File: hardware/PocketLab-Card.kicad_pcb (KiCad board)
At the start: 4 copper layers, 85.6 x 54 mm, 0 parts

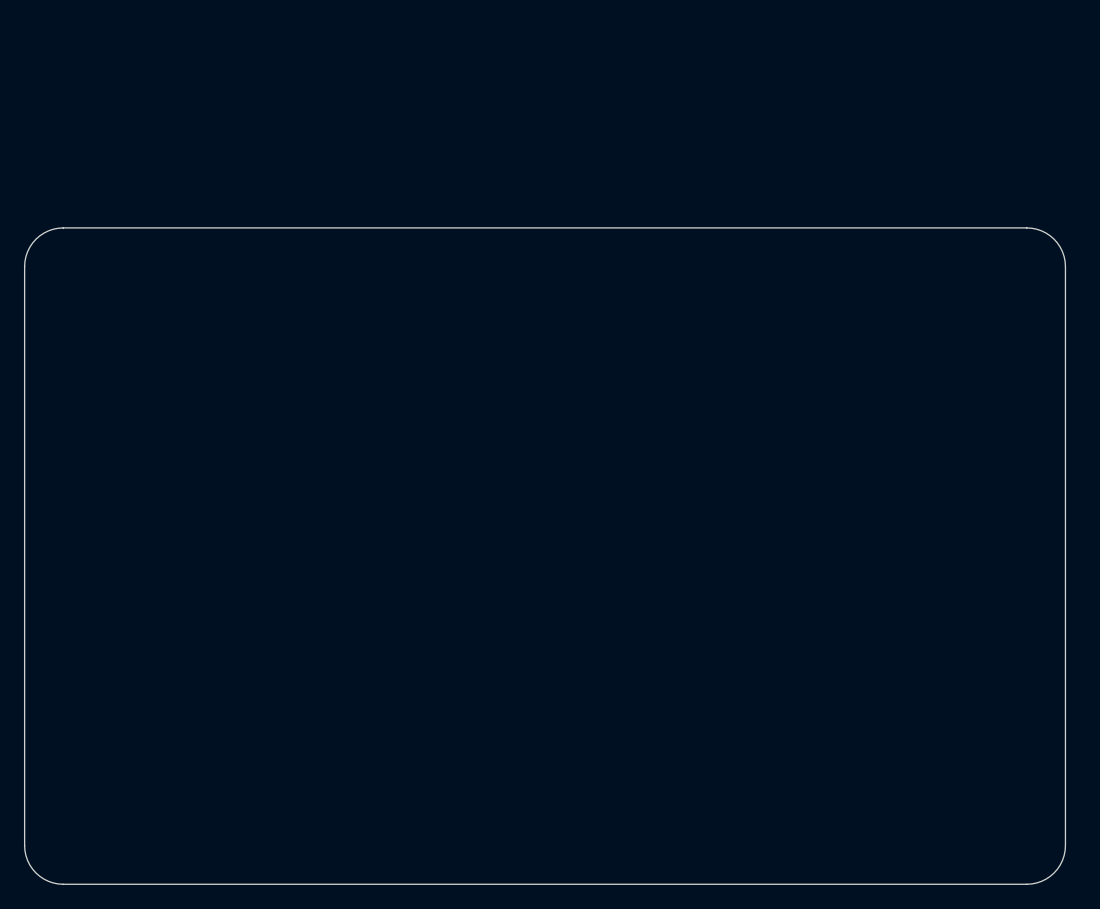
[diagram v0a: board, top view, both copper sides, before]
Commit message: Add physical component placement draft
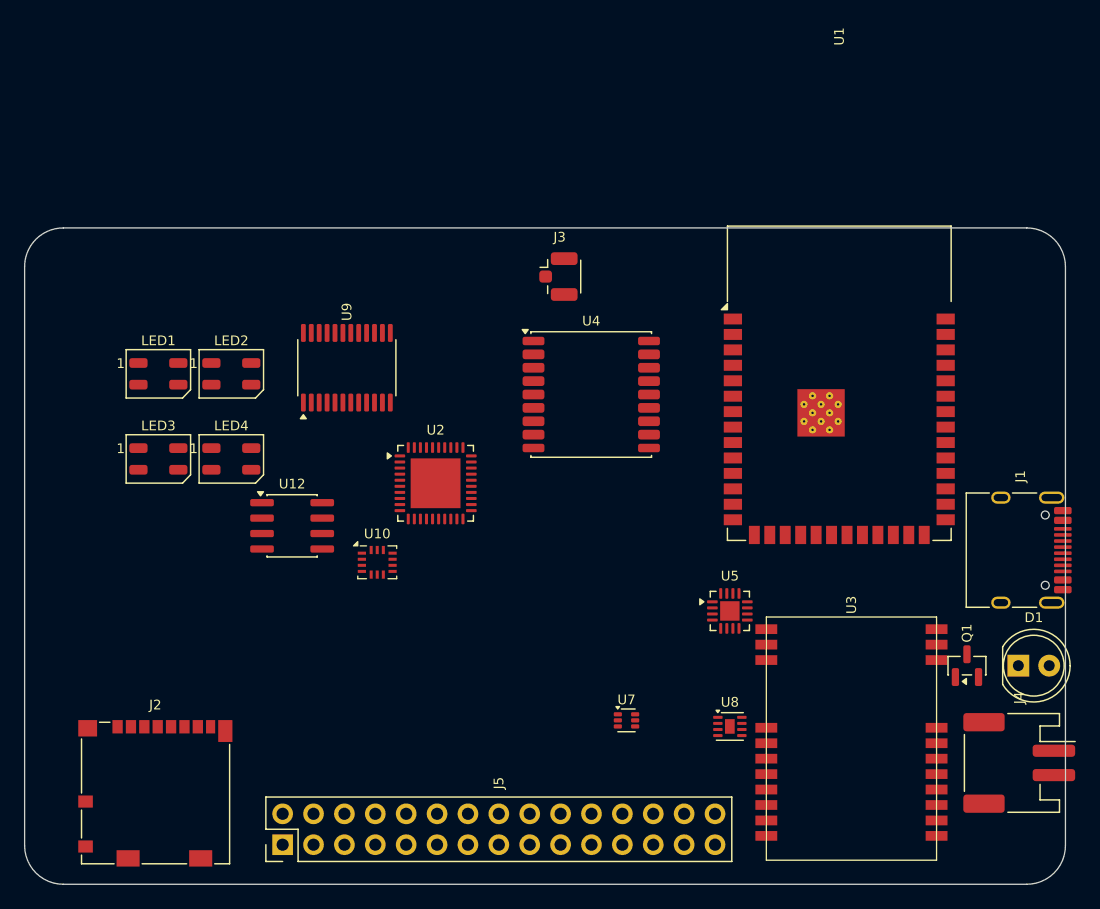
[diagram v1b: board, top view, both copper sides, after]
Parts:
- added D1: TSAL6200 940nm IR (bend toward edge), LED_THT:LED_D5.0mm, F.Cu at (101.7, 56.0)
- added J1: USB-C data/power, Connector_USB:USB_C_Receptacle_HRO_TYPE-C-31-M-12, F.Cu at (101.3, 46.5)
- added J2: microSD, Connector_Card:microSD_HC_Molex_104031-0811, F.Cu at (30.8, 66.5)
- added J3: GNSS ANT, Connector_Coaxial:U.FL_Hirose_U.FL-R-SMT-1_Vertical, F.Cu at (64.4, 24.0)
- added J4: BAT 1S 3.7V, Connector_JST:JST_PH_S2B-PH-SM4-TB_1x02-1MP_P2.00mm_Horizontal, F.Cu at (101.8, 64.0)
- added J5: 2x15 2.54mm EXPANSION, Connector_PinHeader_2.54mm:PinHeader_2x15_P2.54mm_Vertical, F.Cu at (41.2, 70.7)
- added LED1: WS2812B-MINI-V3, LED_SMD:LED_WS2812B-Mini_PLCC4_3.5x3.5mm, F.Cu at (31.0, 32.0)
- added LED2: WS2812B-MINI-V3, LED_SMD:LED_WS2812B-Mini_PLCC4_3.5x3.5mm, F.Cu at (37.0, 32.0)
- added LED3: WS2812B-MINI-V3, LED_SMD:LED_WS2812B-Mini_PLCC4_3.5x3.5mm, F.Cu at (31.0, 39.0)
- added LED4: WS2812B-MINI-V3, LED_SMD:LED_WS2812B-Mini_PLCC4_3.5x3.5mm, F.Cu at (37.0, 39.0)
- added Q1: AO3400A IR driver, Package_TO_SOT_SMD:SOT-23, F.Cu at (97.5, 56.0)
- added U1: ESP32-S3-WROOM-1-N8R2, RF_Module:ESP32-S3-WROOM-1, F.Cu at (87.0, 32.8)
- added U10: BMI270 (FULL option), Package_LGA:Bosch_LGA-14_3x2.5mm_P0.5mm, F.Cu at (49.0, 47.5)
- added U12: PCF8563T, Package_SO:SOIC-8_3.9x4.9mm_P1.27mm, F.Cu at (42.0, 44.5)
- added U2: PN5321A3HN/C106, Package_DFN_QFN:HVQFN-40-1EP_6x6mm_P0.5mm_EP4.1x4.1mm, F.Cu at (53.8, 41.0)
- added U3: E07-900M10S, PocketLab_Custom:E07-900M10S, F.Cu at (81.0, 53.0)
- added U4: MAX-M10S-00B, RF_GPS:ublox_MAX, F.Cu at (66.6, 33.7)
- added U5: BQ24074RGTR, Package_DFN_QFN:VQFN-16-1EP_3x3mm_P0.5mm_EP1.6x1.6mm, F.Cu at (78.0, 51.5)
- added U7: TPS61023DRLR, Package_TO_SOT_SMD:SOT-563, F.Cu at (69.5, 60.5)
- added U8: MAX17048G+T10, Package_DFN_QFN:TDFN-8-1EP_2x2mm_P0.5mm_EP0.8x1.2mm, F.Cu at (78.0, 61.0)
- added U9: TCA9535PWR, Package_SO:TSSOP-24_4.4x7.8mm_P0.65mm, F.Cu at (46.5, 31.5)
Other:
- board text added: "NFC LOOP RESERVE - NOT ROUTED"
- board text added: "PLACEMENT DRAFT - UNROUTED / NOT FOR PRODUCTION"
- board text added: "POWER ISLAND"
- board text added: "U11 BMP390"
- board text added: "U13 IR RX"
- board text added: "U6 TPS63070 + L"
- board text removed: "POCKETLAB CARD V1 - MECHANICAL SCAFFOLD"

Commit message: Publish current PocketLab Card hardware checkpoint
Publishes the current hardware and documentation checkpoint while removing obsolete renders, empty placeholder sheets, generated PCB/autorouter intermediates, and duplicate staging reports. Generated staging artifacts remain reproducible from the checked-in scripts.
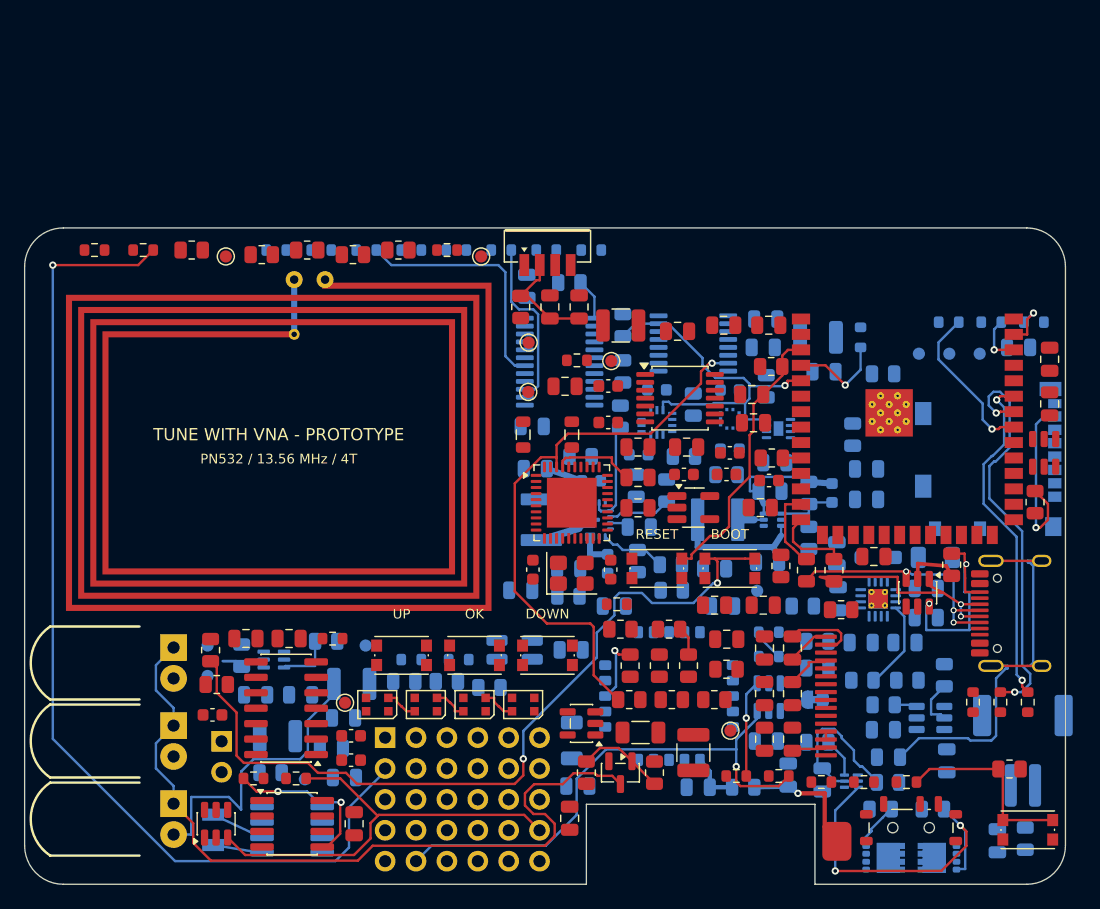
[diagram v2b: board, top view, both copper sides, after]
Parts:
- added A1: T3-868M SPRING ANTENNA, PocketLab_Custom:T3-868M_Edge_Solder, F.Cu at (86.8, 70.5)
- added AE1: PCB NFC LOOP - TUNE ON V1, PocketLab_Custom:NFC_Loop_35x27mm_4T_TUNE, F.Cu at (40.9, 38.0)
- added C101: 4.7nF 1kV, Capacitor_SMD:C_0805_2012Metric, B.Cu at (91.0, 63.5)
- added C102: 100nF, Capacitor_SMD:C_0805_2012Metric, B.Cu at (85.6, 65.4)
- added C103: 4.7uF 10V, Capacitor_SMD:C_0805_2012Metric, B.Cu at (94.2, 52.0)
- added C104: 22uF 10V, Capacitor_SMD:C_0805_2012Metric, B.Cu at (92.4, 54.1)
- added C105: 4.7uF 10V, Capacitor_SMD:C_0805_2012Metric, B.Cu at (86.9, 50.5)
- added C106: 100nF, Capacitor_SMD:C_0805_2012Metric, B.Cu at (94.2, 49.6)
- added C107: 100nF, Capacitor_SMD:C_0805_2012Metric, B.Cu at (70.5, 44.6)
- added C108: 10uF, Capacitor_SMD:C_0805_2012Metric, B.Cu at (62.0, 39.8)
- added C109: 10uF DNP - populate only after VSYS stability test, Capacitor_SMD:C_0805_2012Metric, B.Cu at (80.7, 29.8)
- added C110: 22uF, Capacitor_SMD:C_0805_2012Metric, B.Cu at (60.8, 49.8)
- added C111: 22uF, Capacitor_SMD:C_0805_2012Metric, B.Cu at (61.7, 36.3)
- added C112: 22uF, Capacitor_SMD:C_0805_2012Metric, B.Cu at (68.5, 51.1)
- added C113: 220pF C0G, Capacitor_SMD:C_0603_1608Metric, B.Cu at (86.4, 41.8)
- added C114: 10uF, Capacitor_SMD:C_0805_2012Metric, B.Cu at (81.1, 47.5)
- added C115: 22uF, Capacitor_SMD:C_0805_2012Metric, B.Cu at (81.3, 41.6)
- added C116: 22uF, Capacitor_SMD:C_0805_2012Metric, B.Cu at (77.4, 51.1)
- added C117: 10uF, Capacitor_SMD:C_0805_2012Metric, B.Cu at (90.6, 61.3)
- added C118: 100nF, Capacitor_SMD:C_0805_2012Metric, B.Cu at (100.0, 70.4)
- added C119: 10uF, Capacitor_SMD:C_0805_2012Metric, B.Cu at (95.8, 63.8)
- added C120: 100nF, Capacitor_SMD:C_0805_2012Metric, B.Cu at (81.7, 39.3)
- added C121: 100nF, Capacitor_SMD:C_0805_2012Metric, B.Cu at (88.8, 54.1)
- added C122: 100nF, Capacitor_SMD:C_0805_2012Metric, B.Cu at (86.8, 46.8)
- added C123: 10uF 25V X5R HF, Capacitor_SMD:C_0603_1608Metric, B.Cu at (66.6, 40.8)
- added C124: 10uF 25V X5R HF, Capacitor_SMD:C_0603_1608Metric, B.Cu at (68.0, 47.6)
- added C201: 1uF, Capacitor_SMD:C_0805_2012Metric, F.Cu at (79.8, 33.7)
- added C202: 10uF, Capacitor_SMD:C_0805_2012Metric, F.Cu at (81.2, 28.0)
- added C203: 100nF, Capacitor_SMD:C_0805_2012Metric, F.Cu at (77.5, 28.0)
- added C301: 100nF, Capacitor_SMD:C_0805_2012Metric, F.Cu at (64.4, 33.0)
- added C302: 100nF AVDD, Capacitor_SMD:C_0805_2012Metric, F.Cu at (79.9, 36.0)
- added C303: 4.7uF VBAT bulk, Capacitor_SMD:C_0805_2012Metric, F.Cu at (70.4, 38.0)
- added C304: 100nF, Capacitor_SMD:C_0805_2012Metric, F.Cu at (74.4, 38.0)
- added C305: 100nF, Capacitor_SMD:C_0805_2012Metric, F.Cu at (70.4, 40.5)
- added C306: 22pF C0G, Capacitor_SMD:C_0603_1608Metric, F.Cu at (61.8, 48.1)
- added C307: 22pF C0G, Capacitor_SMD:C_0603_1608Metric, F.Cu at (68.2, 48.1)
- added C308: 220pF C0G, Capacitor_SMD:C_0603_1608Metric, F.Cu at (68.0, 36.0)
- added C309: 220pF C0G, Capacitor_SMD:C_0603_1608Metric, F.Cu at (68.0, 33.0)
- added C310: DNP MATCH, Capacitor_SMD:C_0603_1608Metric, F.Cu at (74.2, 40.3)
- added C311: DNP MATCH, Capacitor_SMD:C_0603_1608Metric, F.Cu at (78.0, 38.5)
- added C312: DNP MATCH, Capacitor_SMD:C_0603_1608Metric, F.Cu at (77.7, 40.3)
- added C313: 10uF DVDD bulk, Capacitor_SMD:C_0805_2012Metric, F.Cu at (70.4, 43.0)
- added C314: 100nF TVDD, Capacitor_SMD:C_0805_2012Metric, F.Cu at (89.8, 47.0)
- added C315: 4.7uF TVDD bulk, Capacitor_SMD:C_0805_2012Metric, F.Cu at (76.7, 51.0)
- added C316: 100nF PVDD, Capacitor_SMD:C_0805_2012Metric, F.Cu at (80.7, 51.0)
- added C317: 100nF VBAT, Capacitor_SMD:C_0805_2012Metric, F.Cu at (77.7, 53.8)
- added C318: 1nF C0G RX COUPLING, Capacitor_SMD:C_0603_1608Metric, F.Cu at (81.2, 40.8)
- added C401: 100nF, Capacitor_SMD:C_0805_2012Metric, B.Cu at (64.7, 48.0)
- added C402: 4.7uF, Capacitor_SMD:C_0805_2012Metric, B.Cu at (76.7, 48.0)
- added C403: DNP SUBGHZ MATCH, Capacitor_SMD:C_0805_2012Metric, B.Cu at (75.4, 66.0)
- added C404: DNP SUBGHZ MATCH, Capacitor_SMD:C_0805_2012Metric, B.Cu at (82.8, 65.0)
- added C501: 100nF HTRC supply, Capacitor_SMD:C_0805_2012Metric, B.Cu at (39.0, 58.4)
- added C502: 10uF HTRC pulse reservoir, Capacitor_SMD:C_0805_2012Metric, B.Cu at (42.7, 58.4)
- added C503: 100nF CEXT, Capacitor_SMD:C_0805_2012Metric, F.Cu at (38.2, 53.8)
- added C504: 100nF QGND, Capacitor_SMD:C_0805_2012Metric, F.Cu at (41.8, 53.8)
- added C505: 100nF C0G COIL ISOLATION, Capacitor_SMD:C_0805_2012Metric, B.Cu at (46.2, 60.3)
- added C506: 3.9nF C0G LF RESONANCE, Capacitor_SMD:C_0805_2012Metric, B.Cu at (45.2, 62.8)
- added C507: 100pF C0G DNP LF TUNE, Capacitor_SMD:C_0603_1608Metric, F.Cu at (46.9, 61.8)
- added C508: 220pF C0G DNP LF TUNE, Capacitor_SMD:C_0603_1608Metric, F.Cu at (46.9, 63.8)
- added C509: 10pF C0G DNP RX EMI, Capacitor_SMD:C_0603_1608Metric, F.Cu at (35.5, 60.0)
- added C510: 100nF, Capacitor_SMD:C_0805_2012Metric, F.Cu at (104.3, 34.5)
- added C511: 10uF, Capacitor_SMD:C_0805_2012Metric, F.Cu at (104.3, 30.8)
- added C512: 47uF 6.3V LOW-ESR, Capacitor_SMD:C_1210_3225Metric, B.Cu at (85.2, 29.0)
- added C513: 100nF OSC supply, Capacitor_SMD:C_0805_2012Metric, B.Cu at (65.0, 54.7)
- added C515: 100nF AHCT supply, Capacitor_SMD:C_0805_2012Metric, F.Cu at (73.7, 28.5)
- added C516: 100nF LVC supply, Capacitor_SMD:C_0805_2012Metric, F.Cu at (80.5, 43.0)
- added C517: 100nF secure element, Capacitor_SMD:C_0805_2012Metric, F.Cu at (47.1, 69.0)
- added C601: 100nF, Capacitor_SMD:C_0805_2012Metric, F.Cu at (63.2, 26.5)
- added C602: 4.7uF, Capacitor_SMD:C_0805_2012Metric, F.Cu at (65.6, 26.5)
- added C603: 100nF, Capacitor_SMD:C_0805_2012Metric, B.Cu at (101.7, 29.8)
- added C604: 100nF, Capacitor_SMD:C_0805_2012Metric, B.Cu at (85.7, 31.8)
- added C605: 100nF, Capacitor_SMD:C_0805_2012Metric, B.Cu at (89.2, 39.8)
- added C606: 100nF, Capacitor_SMD:C_0805_2012Metric, B.Cu at (89.2, 42.3)
- added C607: 22uF 10V X5R IR BUFFER, Capacitor_SMD:C_1206_3216Metric, F.Cu at (70.7, 61.5)
- added C608: 100nF IR HF, Capacitor_SMD:C_0805_2012Metric, F.Cu at (64.8, 68.5)
- added C609: 100nF X7R, Capacitor_SMD:C_0805_2012Metric, B.Cu at (65.5, 65.9)
- added C610: 1uF X7R, Capacitor_SMD:C_0805_2012Metric, F.Cu at (83.2, 54.5)
- added C611: 1uF X7R, Capacitor_SMD:C_0805_2012Metric, F.Cu at (83.2, 58.3)
- added C612: 100nF X7R, Capacitor_SMD:C_0805_2012Metric, F.Cu at (80.8, 54.5)
- added C613: 4.7uF X5R, Capacitor_SMD:C_0805_2012Metric, F.Cu at (80.8, 58.3)
- added C614: 2.2uF X7R, Capacitor_SMD:C_0805_2012Metric, F.Cu at (83.2, 62.0)
- added C615: 4.7uF X5R, Capacitor_SMD:C_0805_2012Metric, F.Cu at (80.8, 62.0)
- added C616: 100nF X7R, Capacitor_SMD:C_0805_2012Metric, B.Cu at (81.0, 62.2)
- added C617: 22uF 10V X5R IR BUFFER, Capacitor_SMD:C_1206_3216Metric, B.Cu at (65.0, 62.1)
- added C701: 100nF, Capacitor_SMD:C_0805_2012Metric, B.Cu at (61.3, 24.8)
- added C702: 100nF, Capacitor_SMD:C_0603_1608Metric, B.Cu at (70.5, 38.6)
- added C703: 100nF, Capacitor_SMD:C_0603_1608Metric, B.Cu at (72.0, 33.3)
- added C704: 100nF, Capacitor_SMD:C_0603_1608Metric, B.Cu at (78.0, 33.3)
- added C705: 100nF, Capacitor_SMD:C_0603_1608Metric, B.Cu at (78.0, 38.2)
- added C706: 100nF, Capacitor_SMD:C_0805_2012Metric, B.Cu at (46.3, 65.2)
- added C707: 100nF, Capacitor_SMD:C_0805_2012Metric, B.Cu at (81.0, 27.5)
- added D101: SMF5.0A, Diode_SMD:D_SOD-123F, B.Cu at (90.2, 47.1)
- added D2: TSAL6200 940nm, PocketLab_Custom:TSAL6200_LayFlat_Inboard, F.Cu at (20.2, 62.2)
- added D3: TSAL6200 940nm, PocketLab_Custom:TSAL6200_LayFlat_Inboard, F.Cu at (20.2, 68.6)
- added F1: Littelfuse 1206L075/13.2, Fuse:Fuse_1206_3216Metric, B.Cu at (94.9, 47.1)
- added J8: ER-OLED0.42-1W 72x40 SSD1306B, PocketLab_Custom:EastRising_ER-OLED0.42-1W_SolderFPC, F.Cu at (90.5, 58.5)
- added L301: 560nH C0G/Q, Inductor_SMD:L_0805_2012Metric, F.Cu at (61.0, 37.0)
- added L302: 560nH C0G/Q, Inductor_SMD:L_0805_2012Metric, F.Cu at (65.0, 37.0)
- added L6: 1.5uH XFL4020-152ME, PocketLab_Custom:Coilcraft_XFL4020, B.Cu at (62.5, 44.0)
- added L7: 1uH HBME042A, PocketLab_Custom:Cyntec_HBME042A-1R0MS, B.Cu at (77.0, 44.0)
- added Q2: CSD16406Q3 DISCHARGE, PocketLab_Custom:CSD16406Q3_VSON-8_3.3x3.3mm_P0.65mm_JLC, B.Cu at (95.2, 71.8)
- added Q3: CSD16406Q3 CHARGE, PocketLab_Custom:CSD16406Q3_VSON-8_3.3x3.3mm_P0.65mm_JLC, B.Cu at (90.7, 71.8)
- added R101: 5.1k 1%, Resistor_SMD:R_0805_2012Metric, B.Cu at (102.3, 70.2)
- added R102: 5.1k 1%, Resistor_SMD:R_0805_2012Metric, F.Cu at (96.2, 47.7)
- added R103: 1M, Resistor_SMD:R_0805_2012Metric, B.Cu at (65.7, 38.8)
- added R104: 330R, Resistor_SMD:R_0805_2012Metric, B.Cu at (91.0, 65.6)
- added R105: 2.2k, Resistor_SMD:R_0805_2012Metric, B.Cu at (85.2, 62.3)
- added R106: 5.1M, Resistor_SMD:R_0805_2012Metric, B.Cu at (94.7, 67.8)
- added R107: 5.1M, Resistor_SMD:R_0805_2012Metric, B.Cu at (90.4, 67.8)
- added R108: 10k TS fixed, Resistor_SMD:R_0805_2012Metric, B.Cu at (74.2, 38.8)
- added R109: 100k, Resistor_SMD:R_0805_2012Metric, B.Cu at (77.7, 40.3)
- added R110: 100k, Resistor_SMD:R_0805_2012Metric, B.Cu at (73.2, 49.8)
- added R111: 3.48k 1%, Resistor_SMD:R_0805_2012Metric, B.Cu at (85.2, 54.0)
- added R112: 3.01k 1%, Resistor_SMD:R_0805_2012Metric, B.Cu at (85.2, 56.2)
- added R113: 1.78k 1%, Resistor_SMD:R_0805_2012Metric, B.Cu at (88.9, 57.2)
- added R114: 68.1k 1%, Resistor_SMD:R_0805_2012Metric, B.Cu at (92.6, 57.2)
- added R115: 100k, Resistor_SMD:R_0805_2012Metric, B.Cu at (64.7, 50.3)
- added R116: 10k, Resistor_SMD:R_0805_2012Metric, B.Cu at (70.3, 41.2)
- added R117: 470k 1%, Resistor_SMD:R_0805_2012Metric, B.Cu at (70.4, 47.4)
- added R118: 150k 1%, Resistor_SMD:R_0805_2012Metric, B.Cu at (73.2, 47.7)
- added R119: 10k, Resistor_SMD:R_0805_2012Metric, B.Cu at (72.8, 41.6)
- added R120: 732k 1%, Resistor_SMD:R_0805_2012Metric, B.Cu at (84.5, 41.8)
- added R121: 100k 1%, Resistor_SMD:R_0805_2012Metric, B.Cu at (84.5, 45.5)
- added R122: 100k, Resistor_SMD:R_0805_2012Metric, B.Cu at (84.0, 51.1)
- added R123: 60.4k 1%, Resistor_SMD:R_0805_2012Metric, B.Cu at (95.6, 56.8)
- added R124: 100k, Resistor_SMD:R_0805_2012Metric, B.Cu at (88.1, 37.0)
- added R125: 10k, Resistor_SMD:R_0805_2012Metric, B.Cu at (81.0, 33.0)
- added R126: 100k, Resistor_SMD:R_0805_2012Metric, B.Cu at (75.0, 34.5)
- added R127: 100k, Resistor_SMD:R_0805_2012Metric, B.Cu at (90.7, 59.2)
- added R128: 100k, Resistor_SMD:R_0805_2012Metric, B.Cu at (90.6, 32.0)
- added R201: 22R, Resistor_SMD:R_0805_2012Metric, F.Cu at (84.3, 48.1)
- added R202: 22R, Resistor_SMD:R_0805_2012Metric, F.Cu at (86.6, 48.1)
- added R203: 10k, Resistor_SMD:R_0805_2012Metric, F.Cu at (81.4, 31.4)
- added R204: 10k, Resistor_SMD:R_0805_2012Metric, F.Cu at (35.3, 54.7)
- added R301: 10k, Resistor_SMD:R_0805_2012Metric, F.Cu at (77.7, 56.3)
- added R302: 10k RESET default asserted, Resistor_SMD:R_0805_2012Metric, F.Cu at (69.7, 58.8)
- added R303: 0R MATCH, Resistor_SMD:R_0805_2012Metric, F.Cu at (47.0, 22.2)
- added R304: 0R MATCH, Resistor_SMD:R_0805_2012Metric, F.Cu at (39.5, 22.2)
- added R305: 2.7k RX TAP, Resistor_SMD:R_0805_2012Metric, F.Cu at (73.2, 58.8)
- added R306: 1k VMID BIAS, Resistor_SMD:R_0805_2012Metric, F.Cu at (76.7, 58.8)
- added R401: 22R, Resistor_SMD:R_0805_2012Metric, F.Cu at (72.2, 56.0)
- added R402: 22R, Resistor_SMD:R_0805_2012Metric, F.Cu at (69.8, 56.0)
- added R403: 22R, Resistor_SMD:R_0805_2012Metric, F.Cu at (69.0, 53.0)
- added R404: 22R, Resistor_SMD:R_0805_2012Metric, F.Cu at (74.6, 56.0)
- added R405: 0R SUBGHZ MATCH, Resistor_SMD:R_0805_2012Metric, B.Cu at (79.1, 66.0)
- added R406: 100k CS SAFE-HIGH, Resistor_SMD:R_0805_2012Metric, F.Cu at (73.0, 53.0)
- added R501: 100R QOD discharge, Resistor_SMD:R_0805_2012Metric, B.Cu at (37.9, 55.2)
- added R502: 47R 0.5W ANTENNA CURRENT LIMIT, Resistor_SMD:R_1210_3225Metric, B.Cu at (40.8, 61.8)
- added R503: 1k LF EMI RETURN, Resistor_SMD:R_0805_2012Metric, B.Cu at (40.2, 64.8)
- added R504: 150k 1% RX DIVIDER, Resistor_SMD:R_0805_2012Metric, F.Cu at (35.8, 57.5)
- added R506: 100k SAFE-OFF, Resistor_SMD:R_0805_2012Metric, B.Cu at (44.8, 54.0)
- added R509: 10k PAIR pull-up, Resistor_SMD:R_0805_2012Metric, F.Cu at (101.0, 64.5)
- added R510: 22R, Resistor_SMD:R_0805_2012Metric, F.Cu at (81.5, 38.9)
- added R511: 22R, Resistor_SMD:R_0805_2012Metric, F.Cu at (87.2, 51.4)
- added R512: 22R, Resistor_SMD:R_0805_2012Metric, F.Cu at (82.2, 47.8)
- added R513: 22R, Resistor_SMD:R_0805_2012Metric, F.Cu at (103.1, 42.5)
- added R514: 47k, Resistor_SMD:R_0805_2012Metric, B.Cu at (51.2, 57.3)
- added R515: 47k, Resistor_SMD:R_0805_2012Metric, B.Cu at (54.7, 57.3)
- added R516: 47k, Resistor_SMD:R_0805_2012Metric, B.Cu at (58.2, 57.8)
- added R517: 47k, Resistor_SMD:R_0805_2012Metric, F.Cu at (33.7, 21.8)
- added R518: 47k, Resistor_SMD:R_0805_2012Metric, F.Cu at (43.2, 21.8)
- added R519: 10k, Resistor_SMD:R_0805_2012Metric, F.Cu at (50.7, 21.8)
- added R601: 39R 0.5W pulse-rated, Resistor_SMD:R_1210_3225Metric, F.Cu at (75.0, 63.1)
- added R602: 100R, Resistor_SMD:R_0805_2012Metric, F.Cu at (66.2, 64.8)
- added R603: 100k, Resistor_SMD:R_0805_2012Metric, F.Cu at (71.8, 64.8)
- added R604: 100R, Resistor_SMD:R_0805_2012Metric, F.Cu at (60.8, 26.5)
- added R605: 68R, Resistor_SMD:R_0603_1608Metric, F.Cu at (89.0, 65.6)
- added R606: 100R PAIR GPIO PROTECTION, Resistor_SMD:R_0603_1608Metric, F.Cu at (92.5, 65.6)
- added R607: 10k, Resistor_SMD:R_0603_1608Metric, F.Cu at (68.7, 51.0)
- added R608: 10k, Resistor_SMD:R_0603_1608Metric, B.Cu at (51.8, 55.5)
- added R609: 10k, Resistor_SMD:R_0603_1608Metric, B.Cu at (55.7, 55.5)
- added R610: 39R 0.5W pulse-rated, Resistor_SMD:R_1210_3225Metric, F.Cu at (69.0, 28.0)
- added R611: 39R 0.5W pulse-rated, Resistor_SMD:R_1210_3225Metric, B.Cu at (46.9, 57.5)
- added R701: 3.3k, Resistor_SMD:R_0805_2012Metric, B.Cu at (69.2, 28.0)
- added R702: 3.3k, Resistor_SMD:R_0805_2012Metric, B.Cu at (69.2, 31.8)
- added R703: 10k, Resistor_SMD:R_0805_2012Metric, B.Cu at (64.8, 24.5)
- added R710: 100R, Resistor_SMD:R_0603_1608Metric, B.Cu at (103.0, 27.8)
- added R711: 100R, Resistor_SMD:R_0603_1608Metric, B.Cu at (99.5, 27.8)
- added R712: 100R, Resistor_SMD:R_0603_1608Metric, B.Cu at (88.8, 29.0)
- added R713: 100R, Resistor_SMD:R_0603_1608Metric, F.Cu at (25.8, 21.8)
- added R714: 100R BOARD TEMP PROBE, Resistor_SMD:R_0603_1608Metric, F.Cu at (29.8, 21.8)
- added R715: 100R, Resistor_SMD:R_0603_1608Metric, B.Cu at (96.0, 27.8)
- added R716: 100R, Resistor_SMD:R_0603_1608Metric, F.Cu at (100.2, 59.0)
- added R717: 100R, Resistor_SMD:R_0603_1608Metric, F.Cu at (102.5, 59.0)
- added R718: 100R, Resistor_SMD:R_0603_1608Metric, F.Cu at (45.3, 53.8)
- added R719: 100R, Resistor_SMD:R_0603_1608Metric, F.Cu at (98.0, 59.0)
- added R720: 100R, Resistor_SMD:R_0603_1608Metric, F.Cu at (54.7, 21.8)
- added R721: 100R, Resistor_SMD:R_0603_1608Metric, F.Cu at (65.4, 30.9)
- added R722: 220R EXPANSION PROTECTION, Resistor_SMD:R_0603_1608Metric, B.Cu at (66.6, 21.8)
- added R723: 220R EXPANSION PROTECTION, Resistor_SMD:R_0603_1608Metric, B.Cu at (62.9, 21.8)
- added R724: 220R EXPANSION PROTECTION, Resistor_SMD:R_0603_1608Metric, B.Cu at (59.2, 21.8)
- added R725: 220R EXPANSION PROTECTION, Resistor_SMD:R_0603_1608Metric, B.Cu at (55.5, 21.8)
- added R726: 220R EXPANSION PROTECTION, Resistor_SMD:R_0603_1608Metric, B.Cu at (51.8, 21.8)
- added R727: 220R EXPANSION PROTECTION, Resistor_SMD:R_0603_1608Metric, B.Cu at (48.1, 21.8)
- added R728: 220R EXPANSION PROTECTION, Resistor_SMD:R_0603_1608Metric, B.Cu at (44.4, 21.8)
- added R729: 220R EXPANSION PROTECTION, Resistor_SMD:R_0603_1608Metric, B.Cu at (40.7, 21.8)
- added R730: 100R, Resistor_SMD:R_0603_1608Metric, F.Cu at (38.8, 65.3)
- added R731: 100R, Resistor_SMD:R_0603_1608Metric, F.Cu at (42.3, 65.3)
- added R732: 100R, Resistor_SMD:R_0603_1608Metric, F.Cu at (78.5, 65.1)
- added R733: 100R, Resistor_SMD:R_0603_1608Metric, F.Cu at (82.0, 65.1)
- added R734: 100R, Resistor_SMD:R_0603_1608Metric, F.Cu at (85.5, 65.6)
- added R735: 100k EN pull-down, Resistor_SMD:R_0805_2012Metric, B.Cu at (69.0, 35.5)
- added R736: 10k 1% BOARD TEMP BIAS, Resistor_SMD:R_0603_1608Metric, B.Cu at (81.2, 53.2)
- added RT701: 10k NTC B3950 1%, Resistor_SMD:R_0603_1608Metric, B.Cu at (81.2, 55.2)
- added SJ1: TS FIXED / CUT FOR EXT NTC, Jumper:SolderJumper-2_P1.3mm_Bridged_RoundedPad1.0x1.5mm, B.Cu at (85.0, 58.8)
- added SW1: RESET, Button_Switch_SMD:SW_Push_1P1T_NO_CK_KMR2, F.Cu at (72.0, 48.0)
- added SW2: BOOT, Button_Switch_SMD:SW_Push_1P1T_NO_CK_KMR2, F.Cu at (78.0, 48.0)
- added SW3: UP, Button_Switch_SMD:SW_Push_1P1T_NO_CK_KMR2, F.Cu at (51.0, 55.1)
- added SW4: DOWN, Button_Switch_SMD:SW_Push_1P1T_NO_CK_KMR2, F.Cu at (63.0, 55.1)
- added SW5: MAIN POWER OFF / ON, Button_Switch_SMD:SW_SPDT_Shouhan_MSK12C02, F.Cu at (92.9, 69.3)
- added SW6: PAIR, Button_Switch_SMD:SW_Push_1P1T_NO_CK_KMR2, F.Cu at (102.5, 69.5)
- added SW7: SELECT, Button_Switch_SMD:SW_Push_1P1T_NO_CK_KMR2, F.Cu at (57.0, 55.1)
- added TP101: BATTERY CELL_POS, TestPoint:TestPoint_Pad_D1.0mm, F.Cu at (36.5, 22.3)
- added TP102: BATTERY CELL_NEG, TestPoint:TestPoint_Pad_D1.0mm, F.Cu at (57.5, 22.3)
- added TP103: BATTERY BAT_FET_MID, TestPoint:TestPoint_Pad_D1.0mm, B.Cu at (80.2, 49.8)
- added TP104: BATTERY GND, TestPoint:TestPoint_Pad_D1.0mm, B.Cu at (35.0, 54.3)
- added TP105: POWER VBUS_USB, TestPoint:TestPoint_Pad_D1.0mm, B.Cu at (48.0, 54.3)
- added TP106: POWER VBUS_FUSED, TestPoint:TestPoint_Pad_D1.0mm, B.Cu at (35.0, 56.8)
- added TP107: POWER VSYS, TestPoint:TestPoint_Pad_D1.0mm, B.Cu at (43.0, 65.3)
- added TP108: POWER +3V3, TestPoint:TestPoint_Pad_D1.0mm, B.Cu at (93.5, 30.3)
- added TP109: POWER +5V_RAW, TestPoint:TestPoint_Pad_D1.0mm, B.Cu at (96.0, 30.3)
- added TP110: POWER +5V_AUX, TestPoint:TestPoint_Pad_D1.0mm, B.Cu at (98.5, 30.3)
- added TP201: JTAG_STRAP_TP, TestPoint:TestPoint_Pad_D1.0mm, F.Cu at (61.4, 33.5)
- added TP202: STRAP_BOOT_TP, TestPoint:TestPoint_Pad_D1.0mm, F.Cu at (68.3, 30.9)
- added TP203: STRAP_VDD_SPI_TP, TestPoint:TestPoint_Pad_D1.0mm, F.Cu at (61.5, 29.4)
- added TP301: NFC_LOADMOD TEST, TestPoint:TestPoint_Pad_D1.0mm, F.Cu at (78.0, 61.3)
- added TP502: LF ANTENNA TAP - HIGH VOLTAGE, TestPoint:TestPoint_Pad_D1.0mm, F.Cu at (46.4, 59.0)
- added U11: BMP390 (FULL OPTION), PocketLab_Custom:BMP390_LGA-10_2x2mm, B.Cu at (78.0, 35.7)
- added U13: TSOP75338WTR 38kHz, PocketLab_Custom:TSOP75338WTR_HeimdallW_SideView, F.Cu at (63.0, 21.5)
- added U14: BQ29700DSE, Package_SON:WSON-6_1.5x1.5mm_P0.5mm, B.Cu at (88.0, 65.5)
- added U15: TPS2553DBVR 500mA LIMIT, Package_TO_SOT_SMD:SOT-23-6, B.Cu at (94.5, 60.3)
- added U16: USBLC6-4SC6Y, Package_TO_SOT_SMD:SOT-23-6, F.Cu at (93.5, 50.0)
- added U17: TPS22919DCKR LF 5V LOAD SWITCH, Package_TO_SOT_SMD:SOT-363_SC-70-6, B.Cu at (40.5, 55.5)
- added U18: TCA9534PWR INTERNAL CONTROL, Package_SO:TSSOP-16_4.4x5mm_P0.65mm, B.Cu at (75.0, 29.5)
- added U19: SRV05-4MR6T1G SD ESD, Package_TO_SOT_SMD:SOT-23-6, F.Cu at (103.8, 38.5)
- added U20: SN74AHCT1G126DBVR RGB LEVEL SHIFT, Package_TO_SOT_SMD:SOT-23-5, F.Cu at (65.8, 60.8)
- added U21: SN74AHCT125PWR LF 3V3-TO-5V, Package_SO:TSSOP-14_4.4x5mm_P0.65mm, F.Cu at (73.9, 34.0)
- added U22: SN74LVC1G17DBVR LF 5V-TO-3V3, Package_TO_SOT_SMD:SOT-23-5_HandSoldering, F.Cu at (75.0, 43.0)
- added U23: ATECC608C-SSHDA-T, Package_SO:SOIC-8_3.9x4.9mm_P1.27mm, F.Cu at (42.0, 69.0)
- added U24: SRV05-4MR6T1G J5 BUS ESD, Package_TO_SOT_SMD:SOT-23-6, F.Cu at (35.8, 69.0)
- added U25: SRV05-4MR6T1G J5 SPI ESD, Package_TO_SOT_SMD:SOT-23-6, B.Cu at (81.2, 58.6)
- added U6: TPS63070RNMR 3V3, PocketLab_Custom:TPS63070_RNM0015A, B.Cu at (67.0, 44.0)
- added Y301: 27.12MHz crystal (pins 2/4 shield), Crystal:Crystal_SMD_3225-4Pin_3.2x2.5mm, F.Cu at (65.0, 48.4)
- added Y501: 4MHz 5V CMOS OSCILLATOR, Oscillator:Oscillator_SMD_EuroQuartz_XO32-4Pin_3.2x2.5mm_RotB_HandSoldering, B.Cu at (60.3, 54.7)
- added Y701: 32.768kHz CL=7pF, Crystal:Crystal_SMD_3215-2Pin_3.2x1.5mm, B.Cu at (35.5, 69.5)
- D1: value TSAL6200 940nm IR (bend toward edge) -> TSAL6200 940nm; footprint LED_THT:LED_D5.0mm -> PocketLab_Custom:TSAL6200_LayFlat_Inboard
- J1: value USB-C data/power -> USB-C DATA/POWER
- J2, U12, U8, U9: moved to B.Cu
- J3: value GNSS ANT -> EXTERNAL 400uH LF COIL; footprint Connector_Coaxial:U.FL_Hirose_U.FL-R-SMT-1_Vertical -> Connector_PinHeader_2.54mm:PinHeader_1x02_P2.54mm_Vertical; moved to B.Cu
- J4: value BAT 1S 3.7V -> PROTECTED 1S LiPo 3.7V; moved to B.Cu
- J5: value 2x15 2.54mm EXPANSION -> 30-PIN 2.54mm DUPONT GRID; footprint Connector_PinHeader_2.54mm:PinHeader_2x15_P2.54mm_Vertical -> PocketLab_Custom:Dupont_Grid_6x5_P2.54mm
- LED1, LED2, LED3, LED4: value WS2812B-MINI-V3 -> WS2812B-2020; footprint LED_SMD:LED_WS2812B-Mini_PLCC4_3.5x3.5mm -> LED_SMD:LED_WS2812B-2020_PLCC4_2.0x2.0mm
- Q1: value AO3400A IR driver -> AO3400A IR DRIVER
- U1: footprint RF_Module:ESP32-S3-WROOM-1 -> PocketLab_Card:ESP32-S3-WROOM-1_PhysicalCourtyard
- U10: value BMI270 (FULL option) -> BMI270 (FULL OPTION); moved to B.Cu
- U3: value E07-900M10S -> E07-900MM10S 855-925MHz; footprint PocketLab_Custom:E07-900M10S -> PocketLab_Custom:E07-900MM10S; moved to B.Cu
- U4: value MAX-M10S-00B -> HTRC11001T/03EE,11 125kHz; footprint RF_GPS:ublox_MAX -> Package_SO:SO-14_3.9x8.65mm_P1.27mm
- U5: footprint Package_DFN_QFN:VQFN-16-1EP_3x3mm_P0.5mm_EP1.6x1.6mm -> Package_DFN_QFN:VQFN-16-1EP_3x3mm_P0.5mm_EP1.6x1.6mm_ThermalVias; moved to B.Cu
- U7: value TPS61023DRLR -> TPS61023DRLR 5V BOOST; moved to B.Cu
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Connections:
- D1 pad 1: (no net) -> /IR_LED_K
- D1 pad 2: (no net) -> /IR_LED_A1
- J1 pad A1: (no net) -> /GND
- J1 pad A12: (no net) -> /GND
- J1 pad A4: (no net) -> /VBUS_USB
- J1 pad A5: (no net) -> /USB_CC1
- J1 pad A6: (no net) -> /USB_CONN_P
- J1 pad A7: (no net) -> /USB_CONN_N
- J1 pad A9: (no net) -> /VBUS_USB
- J1 pad B1: (no net) -> /GND
- J1 pad B12: (no net) -> /GND
- J1 pad B4: (no net) -> /VBUS_USB
- J1 pad B5: (no net) -> /USB_CC2
- J1 pad B6: (no net) -> /USB_CONN_P
- J1 pad B7: (no net) -> /USB_CONN_N
- J1 pad B9: (no net) -> /VBUS_USB
- J1 pad SH: (no net) -> /USB_SHIELD
- J2 pad 1: (no net) -> /SD_DAT2
- J2 pad 10: (no net) -> /SD_DETECT_N
- J2 pad 2: (no net) -> /SD_CS_DEV
- J2 pad 3: (no net) -> /SD_MOSI
- J2 pad 4: (no net) -> /+3V3
- J2 pad 5: (no net) -> /SD_SCK
- J2 pad 6: (no net) -> /GND
- J2 pad 7: (no net) -> /SD_MISO
- J2 pad 8: (no net) -> /SD_DAT1
- J2 pad 9: (no net) -> /GND
- J2 pad SH: (no net) -> /GND
- J3 pad 1: (no net) -> /LF_ANT_A
- J3 pad 2: (no net) -> /LF_ANT_B
- J4 pad 1: (no net) -> /CELL_POS
- J4 pad 2: (no net) -> /CELL_NEG
- J5 pad 1: (no net) -> /+3V3
- J5 pad 10: (no net) -> /GPIO42
- J5 pad 11: (no net) -> /GPIO43
- J5 pad 12: (no net) -> /GPIO44
- J5 pad 13: (no net) -> /GPIO47
- J5 pad 14: (no net) -> /GPIO48
- J5 pad 15: (no net) -> /EX0
- J5 pad 16: (no net) -> /EX1
- J5 pad 17: (no net) -> /EX2
- J5 pad 18: (no net) -> /EX3
- J5 pad 19: (no net) -> /EX4
- J5 pad 2: (no net) -> /GND
- J5 pad 20: (no net) -> /EX5
- J5 pad 21: (no net) -> /EX6
- J5 pad 22: (no net) -> /EX7
- J5 pad 23: (no net) -> /I2C_SDA_HDR
- J5 pad 24: (no net) -> /I2C_SCL_HDR
- J5 pad 25: (no net) -> /SPI_SCK_HDR
- J5 pad 26: (no net) -> /SPI_MOSI_HDR
- J5 pad 27: (no net) -> /SPI_MISO_HDR
- J5 pad 28: (no net) -> /CHG_TS
- J5 pad 29: (no net) -> /+5V_AUX
- J5 pad 3: (no net) -> /GPIO1
- J5 pad 30: (no net) -> /GND
- J5 pad 4: (no net) -> /GPIO2
- J5 pad 5: (no net) -> /GPIO4
- J5 pad 6: (no net) -> /GPIO8
- J5 pad 7: (no net) -> /BOARD_TEMP_HDR
- J5 pad 8: (no net) -> /GPIO40
- J5 pad 9: (no net) -> /GPIO41
- LED1 pad 1: (no net) -> /+5V_RAW
- LED1 pad 2: (no net) -> /RGB_D1_2
- LED1 pad 3: (no net) -> /GND
- LED1 pad 4: (no net) -> /RGB_DIN1
- LED2 pad 1: (no net) -> /+5V_RAW
- LED2 pad 2: (no net) -> /RGB_D2_3
- LED2 pad 3: (no net) -> /GND
- LED2 pad 4: (no net) -> /RGB_D1_2
- LED3 pad 1: (no net) -> /+5V_RAW
- LED3 pad 2: (no net) -> /RGB_D3_4
- LED3 pad 3: (no net) -> /GND
- LED3 pad 4: (no net) -> /RGB_D2_3
- LED4 pad 1: (no net) -> /+5V_RAW
- LED4 pad 2: (no net) -> unconnected-(LED4-DOUT-Pad2)
- LED4 pad 3: (no net) -> /GND
- LED4 pad 4: (no net) -> /RGB_D3_4
- Q1 pad 1: (no net) -> /IR_GATE
- Q1 pad 2: (no net) -> /GND
- Q1 pad 3: (no net) -> /IR_LED_K
- U1 pad 1: (no net) -> /GND
- U1 pad 10: (no net) -> /SD_CS_N
- U1 pad 11: (no net) -> /LF_SCLK_3V3
- U1 pad 12: (no net) -> /GPIO8_MCU
- U1 pad 13: (no net) -> /USB_D_N
- U1 pad 14: (no net) -> /USB_D_P
- U1 pad 15: (no net) -> /JTAG_STRAP_TP
- U1 pad 16: (no net) -> /STRAP_BOOT_TP
- U1 pad 17: (no net) -> /BOARD_TEMP_ADC
- U1 pad 18: (no net) -> /RGB_DATA
- U1 pad 19: (no net) -> /SPI_MOSI
- U1 pad 2: (no net) -> /+3V3
- U1 pad 20: (no net) -> /SPI_SCK
- U1 pad 21: (no net) -> /SPI_MISO
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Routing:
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- added copper zone on In2.Cu, net /+3V3
- added copper zone on In1.Cu, net /GND
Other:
- outline, holes or cut-outs redrawn
- board text added: "+"
- board text added: "-"
- board text added: "868MHz SPRING INSIDE POCKET"
- board text added: "AE1 FULL COMPONENT KEEPOUT - BOTH SIDES"
- board text added: "BOOT"
- board text added: "DOWN"
- board text added: "ESP32 ANTENNA KEEPOUT"
- board text added: "NETLISTED PLACEMENT ONLY - UNROUTED / NOT FOR PRODUCTION"
- board text added: "OK"
- board text added: "RESET"
- board text added: "UP"
- board text removed: "NFC LOOP RESERVE - NOT ROUTED"
- board text removed: "PLACEMENT DRAFT - UNROUTED / NOT FOR PRODUCTION"
- board text removed: "POWER ISLAND"
- board text removed: "U11 BMP390"
- board text removed: "U13 IR RX"
- board text removed: "U6 TPS63070 + L"

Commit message: Route LF RFID analog island
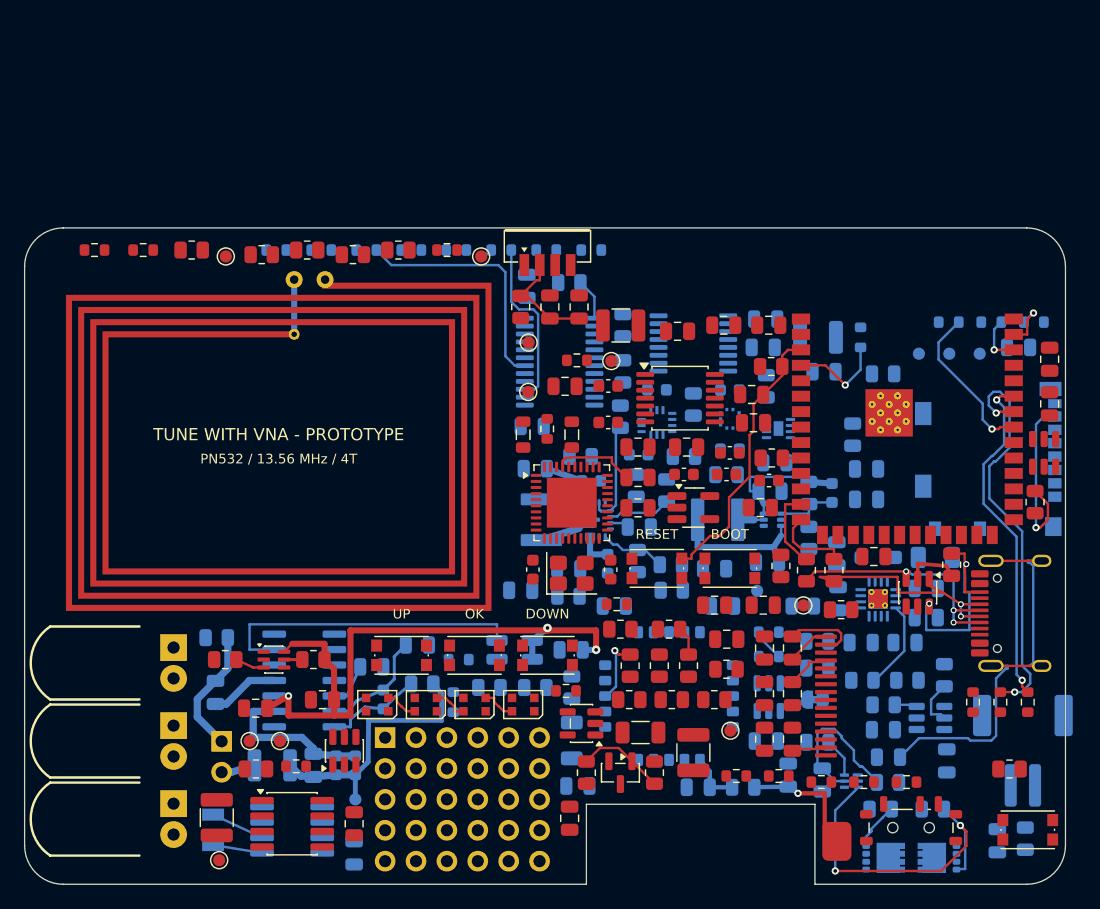
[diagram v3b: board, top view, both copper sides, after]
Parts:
- C501, C502, R501, R506, R611, TP104, TP105, TP106, TP107, U17: moved to F.Cu
- C503, C504, C507, C508, C509, R504, TP502, U4: moved to B.Cu
- moved TP102 44.1 mm to (78.0, 61.3)
- moved R606 41.4 mm to (63.0, 36.5), turned to 90 degrees
- moved R731 36.2 mm to (78.5, 65.1)
- moved TP105 33.4 mm to (57.5, 22.3), turned to 0 degrees
- moved R730 26.7 mm to (64.5, 58.1)
- moved TP104 17.7 mm to (36.0, 72.0), turned to 0 degrees
- moved R504 16.9 mm to (52.7, 57.5), turned to 180 degrees
- moved R611 15.6 mm to (35.8, 68.5), turned to 90 degrees
- moved C509 14.1 mm to (49.5, 58.8), turned to 90 degrees
- moved U24 12.1 mm to (46.3, 63.0)
- moved R503 12.0 mm to (35.8, 53.7)
- moved TP301 11.9 mm to (84.0, 51.0)
- moved R718 10.9 mm to (42.3, 64.3)
- moved R514 10.8 mm to (62.0, 57.8)
- moved C505 10.7 mm to (35.7, 58.2), turned to 90 degrees
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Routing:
- net /BOARD_TEMP_HDR: track 84.4 -> 0.00 mm, vias 1 -> 0
- net /BOOT_N: track 67.1 -> 0.00 mm, vias 2 -> 0
- net /IR_LED_K: track 64.3 -> 0.00 mm
- net /LF_5V: track 0.00 -> 53.0 mm, vias 0 -> 3
- net /NFC_RESET_N: track 47.0 -> 0.00 mm, vias 1 -> 0
- net /I2C_SDA: track 45.0 -> 0.00 mm, vias 3 -> 0
- net /SPI_MOSI_HDR: track 43.2 -> 0.00 mm, vias 1 -> 0
- net /I2C_SCL_HDR: track 36.0 -> 0.00 mm
- net /LF_CLK_4M: track 0.00 -> 25.8 mm
- net /IR_LED_A3: track 24.8 -> 0.00 mm
- net /LF_TAP: track 0.00 -> 21.9 mm
- net /PAIR_N: track 15.6 -> 0.00 mm
- net /LF_TX2: track 0.00 -> 13.1 mm
- net /LF_ANT_A: track 0.00 -> 10.4 mm
- net /LF_QGND: track 0.00 -> 9.08 mm
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
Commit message: Save shared-SPI LF and plane-fanout checkpoint
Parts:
- C515: value 100nF AHCT supply -> 100nF LV-AT supply
- U21: value SN74AHCT125PWR LF 3V3-TO-5V -> SN74LV125ATPWR LF/SPI 3V3-TO-5V IOFF
- U22: value SN74LVC1G17DBVR LF 5V-TO-3V3 -> SN74LVC1G126DBVR LF 5V-TO-3V3 TRI-STATE
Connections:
- U1 pad 11: /LF_SCLK_3V3 -> unconnected-(U1-IO18-Pad11)
- U1 pad 23: /LF_DOUT_3V3 -> unconnected-(U1-IO21-Pad23)
- U1 pad 28: /LF_DIN_3V3 -> unconnected-(U1-IO35-Pad28)
- U21 pad 2: /LF_SCLK_3V3 -> /SPI_MOSI
- U21 pad 3: /LF_SCLK_5V -> /LF_DIN_5V
- U21 pad 5: /LF_DIN_3V3 -> /SPI_SCK
- U21 pad 6: /LF_DIN_5V -> /LF_SCLK_5V
- U22 pad 1: unconnected-(U22-NC-Pad1) -> /LF_RFID_EN
- U22 pad 4: /LF_DOUT_3V3 -> /SPI_MISO
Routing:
- net /GND: track 4.54 -> 328.8 mm, vias 0 -> 136
- net /+3V3: track 2.90 -> 127.9 mm, vias 0 -> 55

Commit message: Save PCBA routing optimization checkpoint
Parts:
- added R129: 0R SPI CROSSOVER, Resistor_SMD:R_0805_2012Metric, B.Cu at (84.2, 49.1)
- moved R122 8.75 mm to (89.8, 44.5), turned to 0 degrees
- moved J2 0.18 mm to (99.1, 39.0)
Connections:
- R402 pad 1: /SPI_MOSI -> /SPI_MOSI_JMP
- U21 pad 10: /LF_5V -> /GND
- U21 pad 11: unconnected-(U21-Pin_11-Pad11) -> /LF_DIN_5V
- U21 pad 12: /GND -> /SPI_MOSI
- U21 pad 13: /LF_5V -> /GND
- U21 pad 2: /SPI_MOSI -> /GND
- U21 pad 3: /LF_DIN_5V -> unconnected-(U21-Pin_3-Pad3)
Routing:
- net /+3V3: track 127.9 -> 303.9 mm, vias 55 -> 63
- net /LF_RFID_EN: track 2.39 -> 109.6 mm, vias 0 -> 1
- net /SUBGHZ_GDO2: track 0.00 -> 72.8 mm, vias 0 -> 6
- net /LF_DIN_5V: track 0.00 -> 71.9 mm, vias 0 -> 3
- net /LF_DOUT_5V: track 0.00 -> 62.8 mm, vias 0 -> 1
- net /GND: track 328.8 -> 391.2 mm, vias 136 -> 133
- net /LF_5V: track 53.0 -> 113.5 mm
- net /I2C_SCL_HDR: track 0.00 -> 52.4 mm, vias 0 -> 2
- net /AUX5_EN: track 1.85 -> 50.9 mm, vias 0 -> 4
- net /AUX5_FAULT_N: track 0.00 -> 48.8 mm, vias 0 -> 2
- net /LF_SCLK_5V: track 0.00 -> 46.9 mm, vias 0 -> 3
- net /+5V_RAW: track 11.0 -> 56.6 mm, vias 0 -> 19
- net /SPI_SCK: track 0.00 -> 42.6 mm, vias 0 -> 2
- net /CHG_ILIM: track 0.00 -> 37.0 mm, vias 0 -> 4
- net /CELL_NEG: track 0.00 -> 36.1 mm, vias 0 -> 5
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- added copper zone on In2.Cu, net /+5V_AUX
- added copper zone on In2.Cu, net /+5V_RAW

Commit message: Advance reviewed PCB routing checkpoint
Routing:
- net /LF_RFID_EN: track 109.6 -> 155.5 mm, vias 1 -> 2
- net /SPI_SCK_HDR: track 21.0 -> 63.9 mm, vias 1 -> 2
- net /USB_CC1: track 0.00 -> 33.4 mm, vias 0 -> 1
- net /SPI_MOSI: track 24.6 -> 54.5 mm, vias 3 -> 5
- net /I2C_SDA_HDR: track 0.00 -> 21.7 mm, vias 0 -> 1
- net /USER_BUTTON_A_N: track 4.44 -> 21.6 mm, vias 0 -> 2
- net /+3V3: track 303.9 -> 291.0 mm, vias 63 -> 61
- net /I2C_SCL: track 1.47 -> 8.41 mm, vias 1 -> 3
- net /NFC_TX2_F: track 0.00 -> 4.83 mm
- net /CELL_POS: track 23.4 -> 27.6 mm
- net /SD_CS_DEV: track 0.00 -> 3.97 mm, vias 0 -> 1
- net /FG_ALERT_N: track 4.30 -> 6.56 mm, vias 0 -> 2
- net /I2C_SDA: track 14.2 -> 16.5 mm
- net /+5V_RAW: track 56.6 -> 58.3 mm
- net /GND: track 391.2 -> 392.6 mm

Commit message: Route protected GPIO43 to expansion header
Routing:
- net /GPIO43: track 0.00 -> 17.7 mm, vias 0 -> 1
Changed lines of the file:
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@@
 		(net "/U6_PS_SYNC")
+	)
+	(via
+		(at 43.05 64.224999)
+		(size 0.45)
+		(drill 0.2)
+		(layers "F.Cu" "B.Cu")
+		(locked yes)
+		(net "/GPIO43")
+	)
+	(segment
+		(start 43.05 64.224999)
+		(end 44.235 63.19)
+		(width 0.15)
+		(locked yes)
+		(layer "In2.Cu")
+		(net "/GPIO43")
+	)
+	(segment
+		(start 44.235 63.19)
+		(end 58.54 63.19)
+		(width 0.15)
+		(locked yes)
+		(layer "In2.Cu")
+		(net "/GPIO43")
+	)
+	(segment
+		(start 58.54 63.19)
+		(end 59.81 64.459999)
+		(width 0.15)
+		(locked yes)
+		(layer "In2.Cu")
+		(net "/GPIO43")
 	)
 	(segment
